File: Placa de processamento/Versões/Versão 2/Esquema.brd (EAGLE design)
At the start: 145.1 x 79.8 mm, 17 parts, among them IC1 5V, IC2 5V

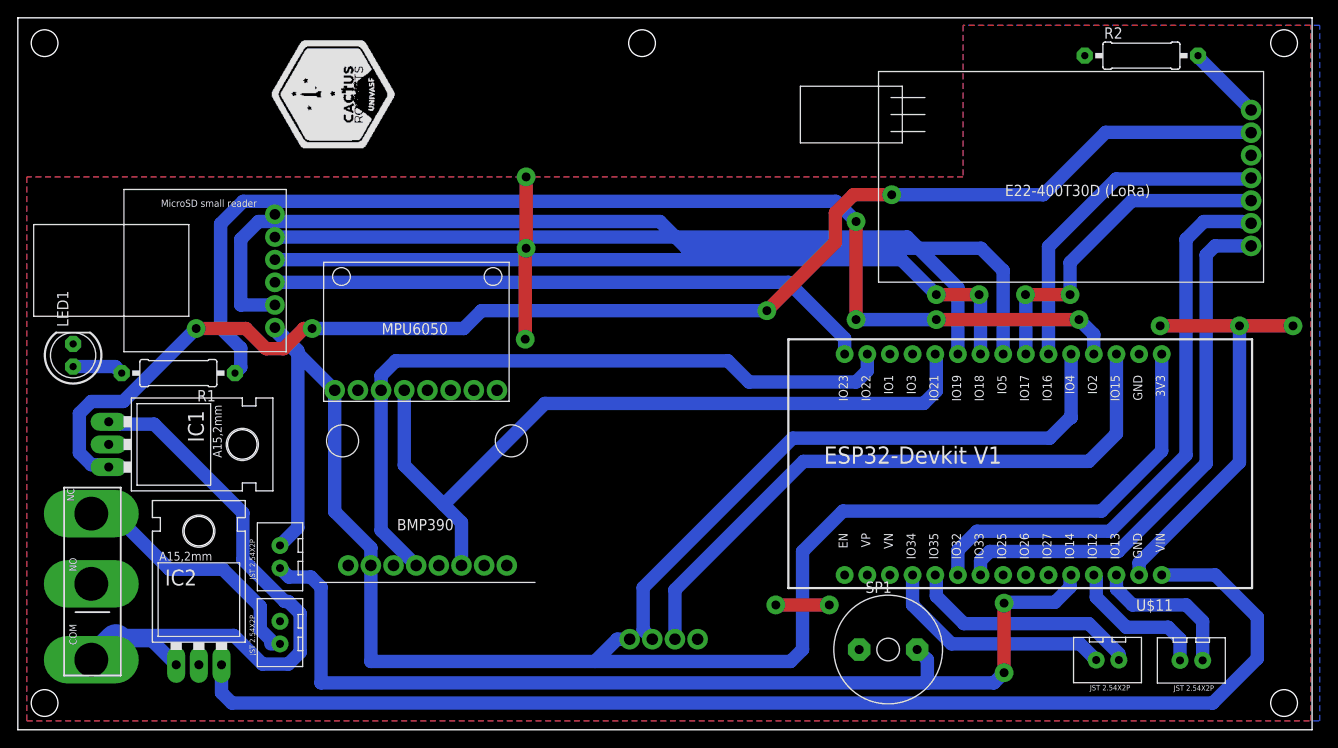
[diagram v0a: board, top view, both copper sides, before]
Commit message: resolved erros in pcb layout
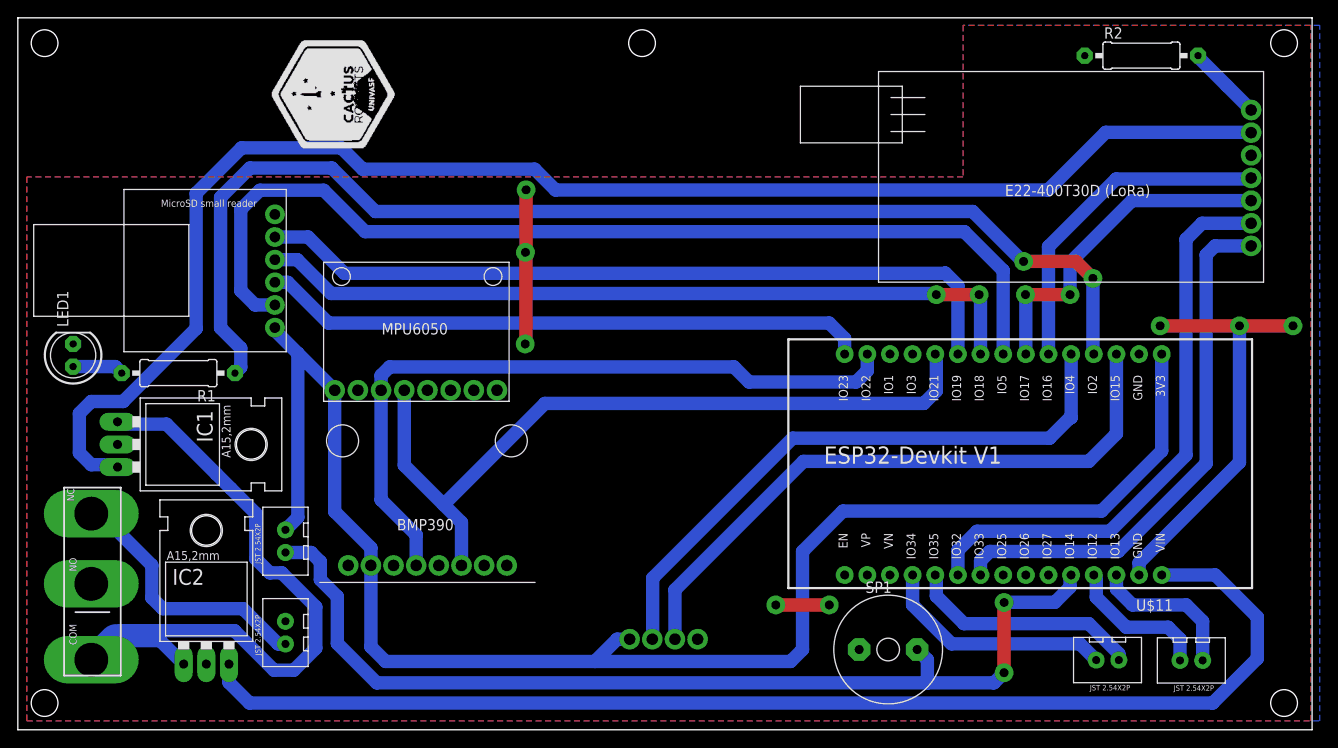
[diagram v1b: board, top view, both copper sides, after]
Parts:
- moved U$4 1.86 mm to (30.0, 21.1)
- moved IC1 0.99 mm to (15.0, 32.0)
- moved IC2 0.84 mm to (21.1, 11.2)
- moved U$7 0.61 mm to (30.0, 10.9)
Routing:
- net VOUT_LORA: track 156.6 -> 166.6 mm, vias 4 -> 0
- net 3V3: track 188.9 -> 182.0 mm
- net VIN: track 75.8 -> 80.2 mm
- net CS: track 109.2 -> 113.1 mm
- net LED1: track 131.7 -> 133.8 mm, vias 4 -> 2
- net BUZZER: track 114.9 -> 113.0 mm
- net VOUT: track 139.2 -> 137.7 mm
- net V_BATTERY: track 28.5 -> 30.0 mm
- net GND: track 71.7 -> 70.9 mm
- net TX1: track 69.2 -> 68.4 mm
- net SCL: track 81.5 -> 80.9 mm

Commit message: resolved layout position
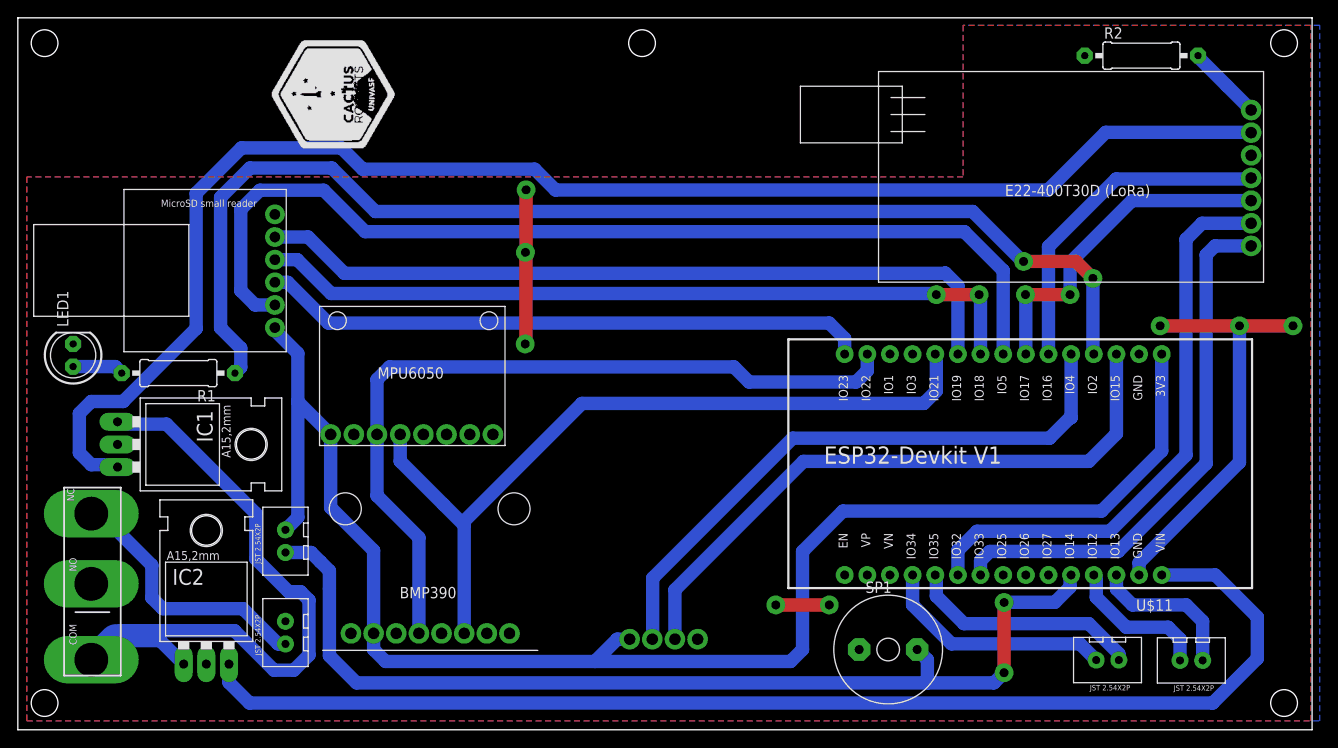
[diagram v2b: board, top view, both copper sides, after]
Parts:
- moved U$1 7.63 mm to (45.9, 19.2)
- moved U$9 4.97 mm to (44.0, 43.3)
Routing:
- net SCL: track 80.9 -> 89.1 mm
- net 3V3: track 182.0 -> 176.6 mm
- net SDA: track 87.0 -> 88.9 mm
- net BUZZER: track 113.0 -> 114.3 mm
- net VIN: track 80.2 -> 79.5 mm
